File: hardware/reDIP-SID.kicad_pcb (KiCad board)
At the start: 4 copper layers, 17.8 x 35.6 mm, 92 parts, among them J1 Conn_01x04, J2 Conn_01x04, J3 Conn_01x10, J4 Conn_01x10, J5 TYPE-C-31-M-12, J6 Conn_02x05_Odd_Even, Q1 PDTA143ZMB, SW1 KXT331LHS, U1 NCP163AMX120TBG, U2 NCP167AMX330TBG, U3 SN74CBTD16211DGVR, U4 SGTL5000XNLA3, U5 NUF2042XV6, U6 APS6404L-3SQR-SN, U7 W25Q128JVPIM, U8 ICE40UP5K-SG48I, X1 ASCO-24.576MHZ-EK-T

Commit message: Removed splits in ground on layer In2.Cu, removed ground pour on layer B.Cu
Changes suggested by zyp.
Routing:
- net /SPI_SIO0: track 48.6 -> 50.6 mm
- net /SPI_SCLK: track 28.7 -> 30.2 mm
- removed copper zone on B.Cu, net GND

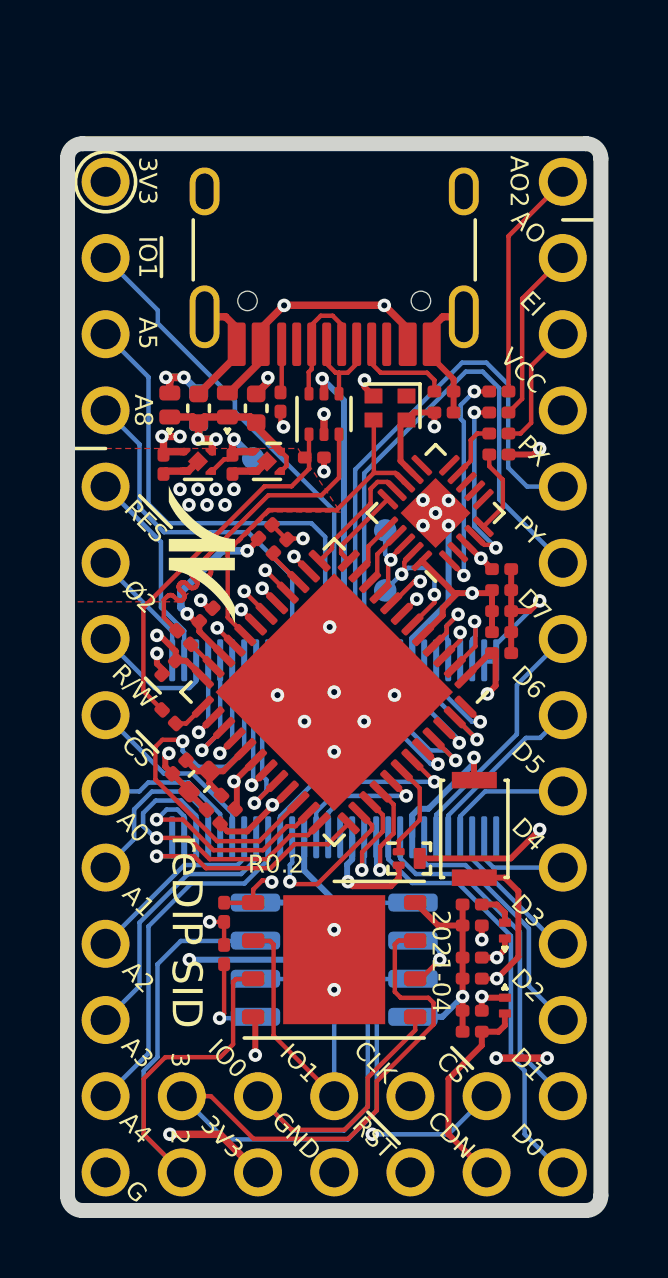
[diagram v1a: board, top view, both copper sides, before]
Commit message: Small cleanups
* Removed ground split under USB D-
* More ground fill on layer In2.Cu, in the vicinity of SPI traces
* Slight improvents to SPI routing
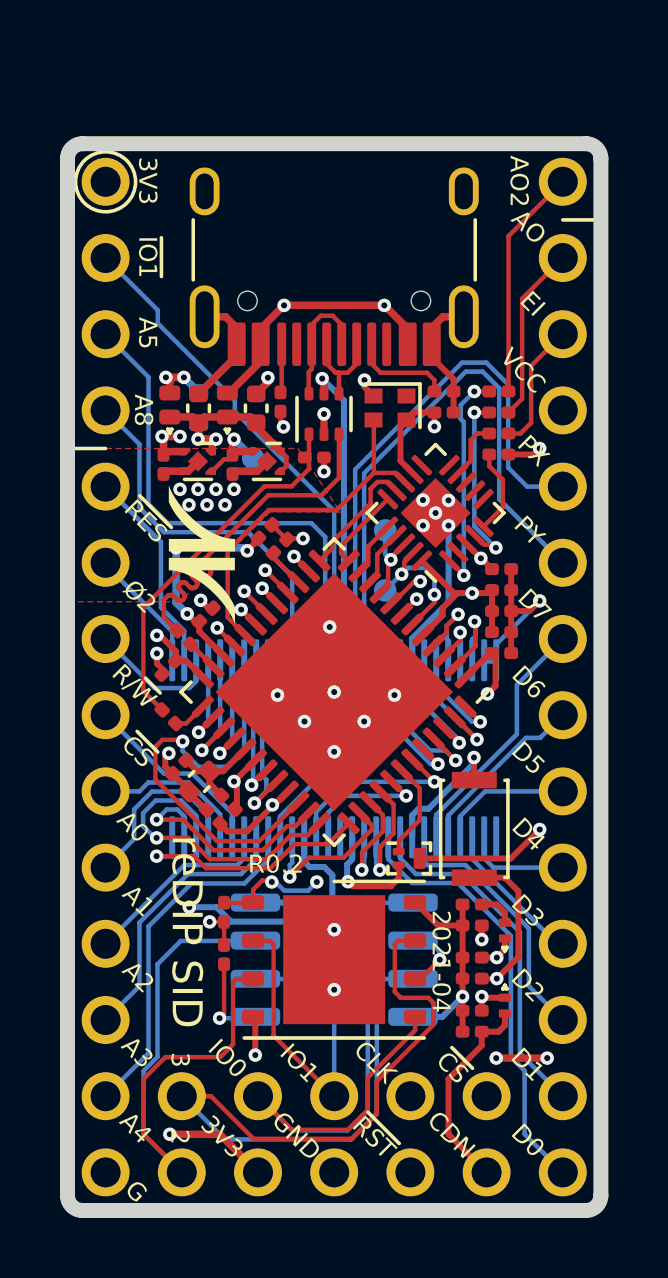
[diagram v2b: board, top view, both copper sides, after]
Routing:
- net /SPI_SIO0: track 50.6 -> 48.8 mm
- net /SPI_FLASH_~CS~: track 31.2 -> 32.6 mm
- net +5V: track 38.6 -> 37.6 mm
- net +3V3: track 37.3 -> 37.1 mm, vias 14 -> 15

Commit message: Showstopper fixes
* Pins swaps and rerouting to handle the fact that iCE40UP5K pins 35 and 37
  are output only when the PLL is used
* Removed Q1, USB_CONN is now used to pull up USB D+ directly through R3
* Changed the oscillator to 24 MHz (full speed USB is clocked at 12 MHz)
* Slight rounding of footprint pads for oscillator and button

Many thanks go to @smunaut for pointing out the (undocumented!) iCE40 PLL
peculiarities, and to zyp for pointing out that the PLL can't convert a
24.576MHz clock to anything that will work for full speed USB.
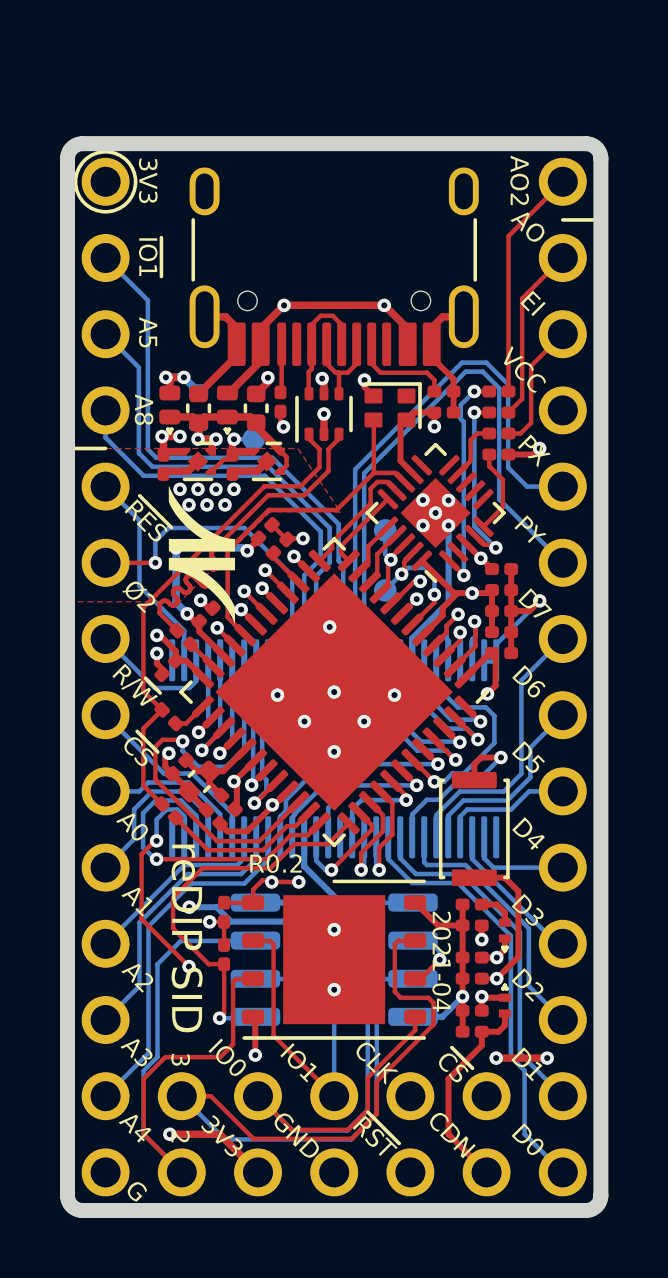
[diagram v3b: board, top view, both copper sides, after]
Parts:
- removed Q1: PDTA143ZMB, Nexperia:SOT-883
- SW1: footprint Button_Switch_SMD:SW_SPST_CK_KXT3 -> CK:SW_SPST_CK_KXT3
- U1: value NCP163AMX120TBG -> NCP115AMX120TCG
- X1: value ASCO-24.576MHZ-EK-T -> ASCO-24.000MHZ-EK-T3; footprint Oscillator:Oscillator_SMD_Abracon_ASCO-4Pin_1.6x1.2mm -> reDIP:Oscillator_SMD-4Pin_1.6x1.2mm
- moved R3 12.7 mm to (102.1, 121.0), turned to 315 degrees
- moved TP1 0.64 mm to (104.9, 108.6)
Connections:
- R3 pad 2: /USB_LINK -> /USB_CONN
- U3 pad 13: /USB_3V3 -> /ICE_~IO1~
- U3 pad 15: /ICE_~IO1~ -> /ICE_A5
- U3 pad 16: /ICE_A5 -> /ICE_A8
- U3 pad 18: /ICE_A8 -> /ICE_Ø2
- U3 pad 28: /ICE_Ø2 -> (no net)
- U3 pad 29: /Ø2 -> (no net)
- U3 pad 39: /A8 -> /Ø2
- U3 pad 40: /A5 -> /A8
- U3 pad 41: /~IO1~ -> /A5
- U3 pad 43: VBUS -> /~IO1~
- U8 pad 21: /SPI_RAM_~CS~ -> /ICE_~RES~
- U8 pad 35: /ICE_~RES~ -> /USB_CONN
- U8 pad 37: /ICE_Ø2 -> /SPI_RAM_~CS~
- U8 pad 42: /USB_~CONN~ -> /ICE_A5
- U8 pad 43: /ICE_A5 -> /ICE_D6
- U8 pad 44: /ICE_D0 -> /ICE_Ø2
- U8 pad 45: /ICE_D1 -> /ICE_D0
- U8 pad 46: /ICE_D2 -> /ICE_D1
- U8 pad 47: /ICE_D7 -> /ICE_D2
- U8 pad 48: /ICE_D6 -> /ICE_D7
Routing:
- net /USB_LINK: track 22.2 -> 0.00 mm, vias 2 -> 0
- net /ICE_~RES~: track 7.87 -> 22.3 mm, vias 1 -> 3
- net VBUS: track 19.0 -> 9.23 mm
- net /Ø2: track 4.17 -> 10.6 mm, vias 0 -> 1
- net /SPI_RAM_~CS~: track 19.0 -> 13.1 mm, vias 2 -> 1
- net /USB_CONN: track 0.00 -> 5.42 mm
- net /ICE_D6: track 3.49 -> 7.65 mm
- net /USB_D+: track 12.4 -> 16.4 mm
- net /USB_3V3: track 3.86 -> 0.00 mm, vias 1 -> 0
- net /USB_~CONN~: track 3.31 -> 0.00 mm
- net /~IO1~: track 17.4 -> 19.0 mm
- net GND: track 49.5 -> 51.1 mm
- net /ICE_A8: track 5.48 -> 3.96 mm
- net /ICE_Ø2: track 8.34 -> 6.98 mm
- net /A8: track 12.5 -> 13.9 mm
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
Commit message: Preparing for prototyping
* Routing cleanups
* Changed oscillator to ± 25 ppm part
* Note on the PLL output-only-pin trap in the schematic

Thanks to @DX-MON for pointing out that audio hardware should have
as high frequency stability as possible.
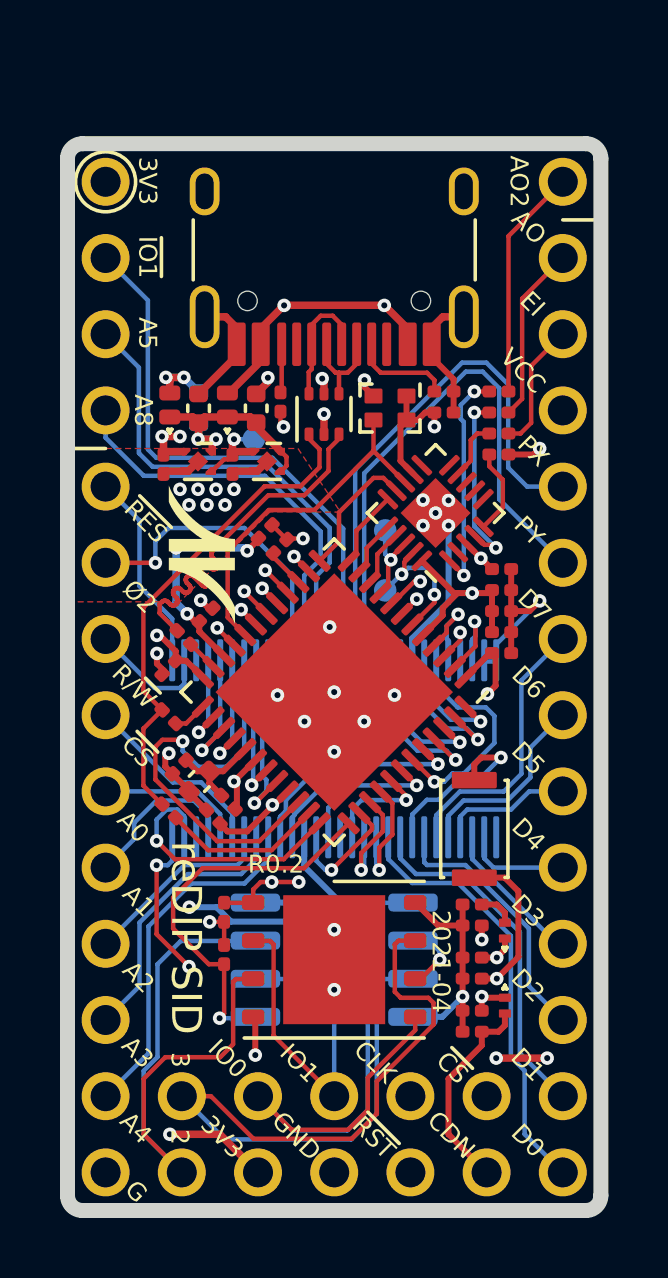
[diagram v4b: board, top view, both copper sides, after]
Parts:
- X1: value ASCO-24.000MHZ-EK-T3 -> ECS-1612MV-240-CN-TR
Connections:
- U3 pad 26: /ICE_R_~W~ -> (no net)
- U3 pad 27: /ICE_~RES~ -> /ICE_R_~W~
- U3 pad 28: (no net) -> /ICE_~RES~
- U3 pad 29: (no net) -> /~RES~
- U3 pad 30: /~RES~ -> /R_~W~
- U3 pad 31: /R_~W~ -> (no net)
- X1 pad 1: (no net) -> +3V3
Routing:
- net /ICE_~RES~: track 22.3 -> 19.8 mm
- net /ICE_R_~W~: track 10.6 -> 8.74 mm
- net GND: track 51.1 -> 49.4 mm
- net +3V3: track 37.1 -> 37.9 mm
- net /A1: track 6.12 -> 5.61 mm

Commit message: Improved decoupling
* Improved decoupling and PLL power filtering, as suggested by @smunaut
* Minor cleanups on F.Fab layer
* Added note in the schematic on the side effects of pressing the user button
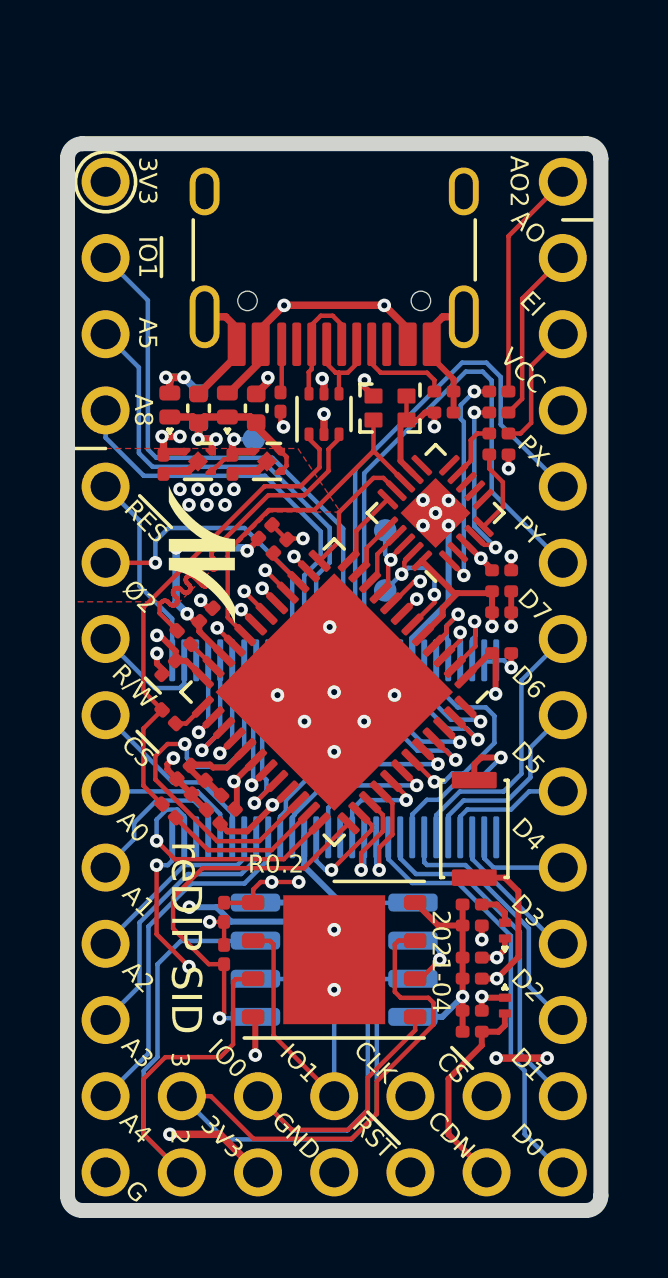
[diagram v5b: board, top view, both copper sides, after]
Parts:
- removed the C17 at (113.2, 115.0)
- removed the C20 at (103.1, 120.0)
- added C19: 1uF, Capacitor_SMD:C_0201_0603Metric, F.Cu at (103.1, 120.2)
- moved C15 0.74 mm to (113.2, 114.3)
- moved C16 0.66 mm to (113.2, 113.7)
- moved C18 0.23 mm to (102.6, 119.7)
- renumbered C18 to C17, C19 to C18, C21 to C20
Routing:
- net GND: track 49.4 -> 44.9 mm, vias 34 -> 36
- net +1V2: track 34.8 -> 35.7 mm
- net /POT_X: track 18.1 -> 17.4 mm

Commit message: Files for manufacture
* Added note on pin-in-paste for USB-C connector
* Capped component position resolution to 0.01mm
* Moved kicost BOM spreadsheet to documentation/
* Files for fabrication and assembly generated by KiKit
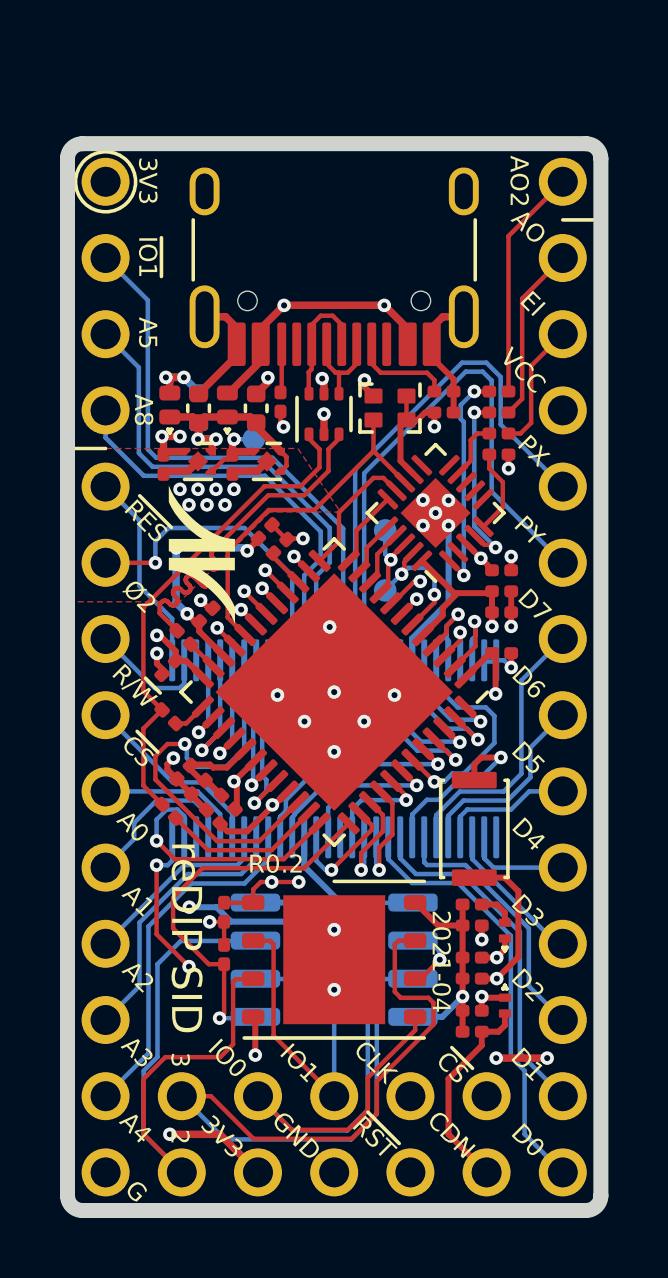
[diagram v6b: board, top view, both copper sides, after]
